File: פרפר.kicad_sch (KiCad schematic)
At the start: 41 parts, among them J1 JST_SH_BM03B-SRSS-TB, J2 Hirose_FH12-22S-0.5SH, J5 JST_SH_SM04B-SRSS-TB, J6 JST_SUR_SM02B-SURS-TF, J7 JST_SH_BM03B-SRSS-TB

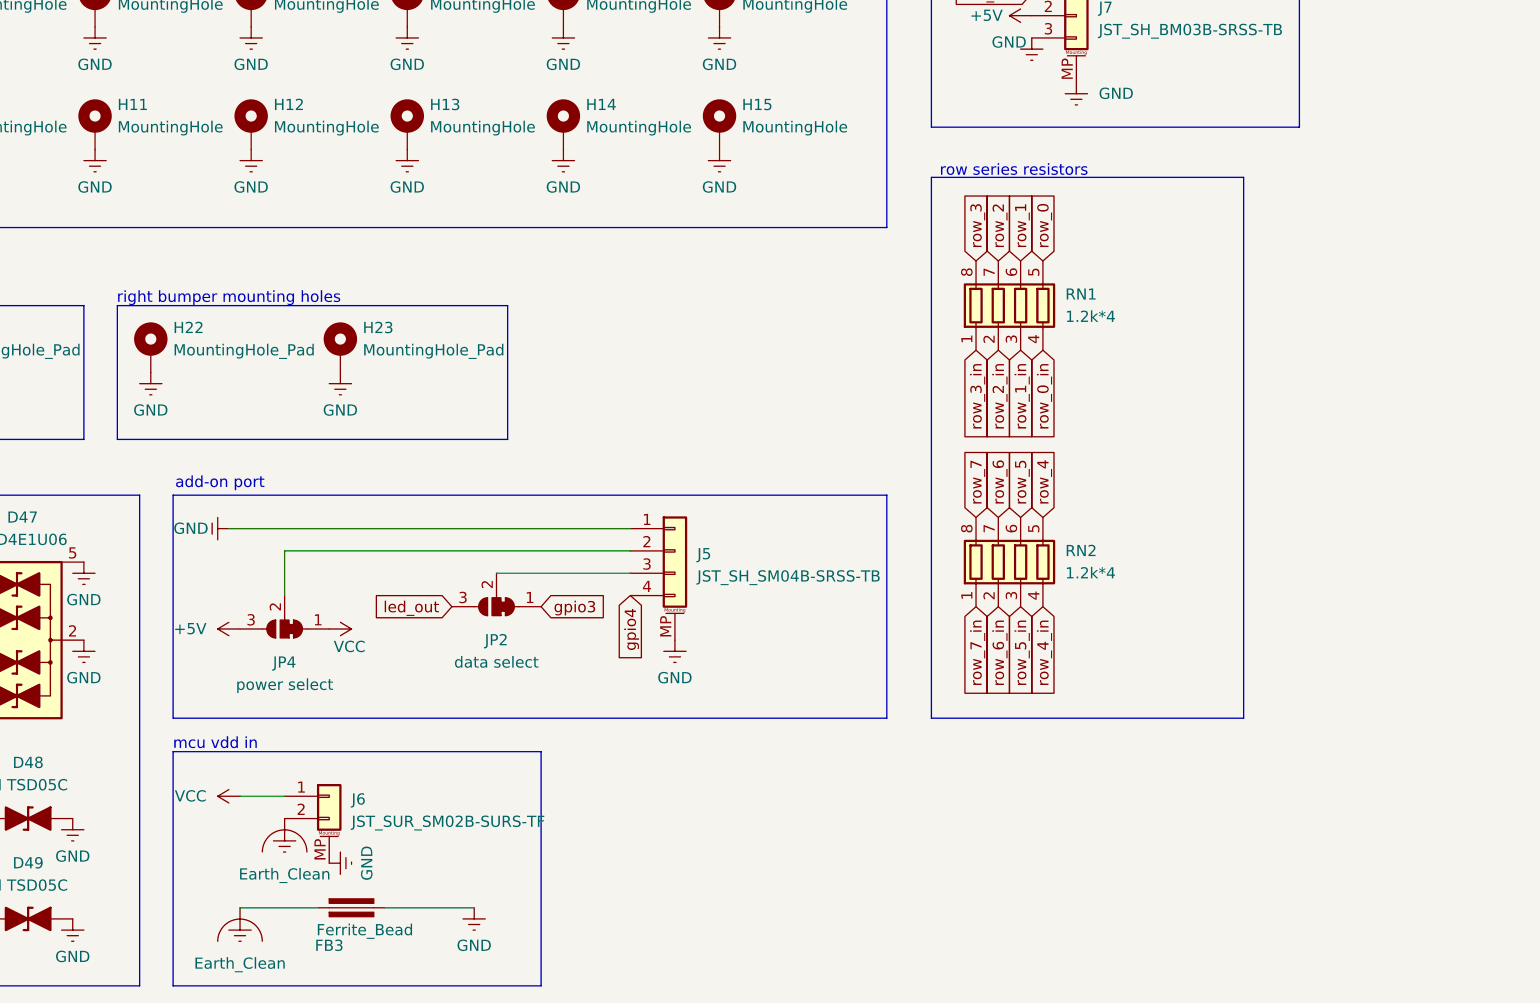
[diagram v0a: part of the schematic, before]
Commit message: column resistors to further bolster protection against esd events and shorts
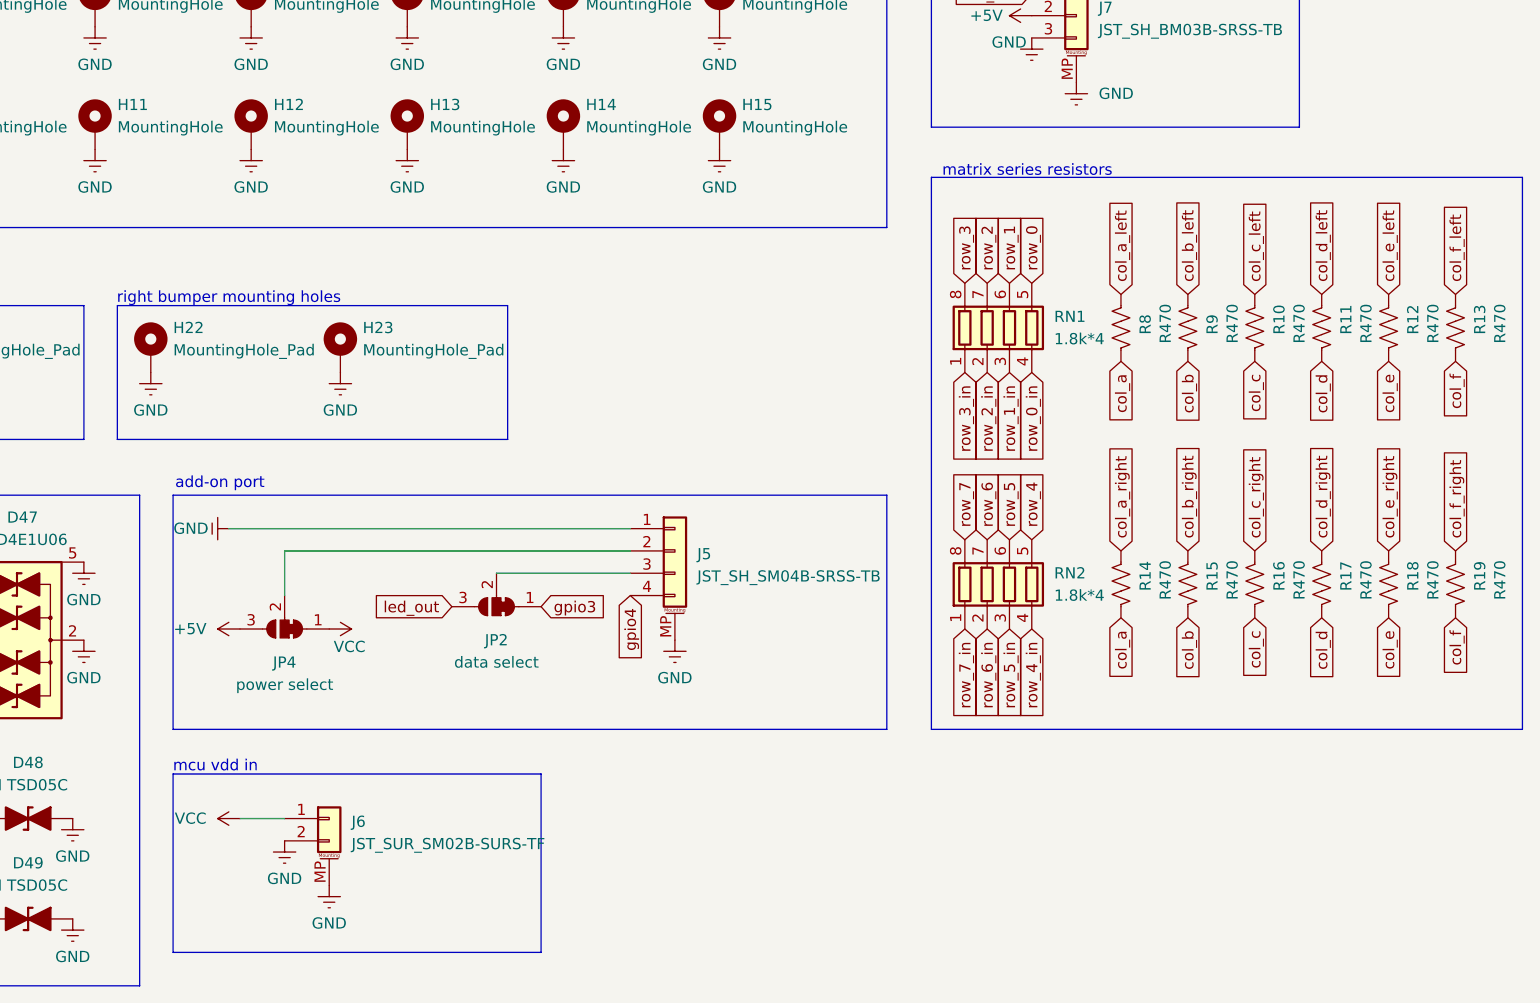
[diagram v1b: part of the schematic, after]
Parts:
- removed FB3: Ferrite_Bead, PCM_Ferrite_SMD_AKL:Ferrite_0805_2012Metric, symbol PCM_Device_AKL:Ferrite_Bead
- added R10, R11, R12, R13, R14, R15, R16, R17, R18, R19, R8, R9: R470, Resistor_SMD:R_0805_2012Metric, symbol Device:R_US
- RN1, RN2: value 1.2k*4 -> 1.8k*4
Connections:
- net Earth_Clean is gone; now on net GND: J6.2 (Pin_2)
- net col_a: now also R14.1, R8.1
- net col_b: now also R15.1, R9.1
- net col_c: now also R10.1, R16.1
- net col_d: now also R11.1, R17.1
- net col_e: now also R12.1, R18.1
- net col_f: now also R13.1, R19.1
- new net col_a_left: R8.2
- new net col_a_right: R14.2
- new net col_b_left: R9.2
- new net col_b_right: R15.2
- new net col_c_left: R10.2
- new net col_c_right: R16.2
- new net col_d_left: R11.2
- new net col_d_right: R17.2
- new net col_e_left: R12.2
- new net col_e_right: R18.2
- new net col_f_left: R13.2
- new net col_f_right: R19.2
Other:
- note added: "matrix series resistors"
- note removed: "row series resistors"
- moved on the sheet: J6, RN1, RN2

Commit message: actually production version, for real?
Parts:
- R10, R11, R12, R13, R14, R15, R16, R17, R18, R19, R8, R9: value R470 -> R220
- RN1, RN2: value 1.8k*4 -> R390*4
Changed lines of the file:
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@@
 	(title_block
 		(title "coquette switch matrix (parpar)")
-		(date "2025-01-20")
+		(date "2025-01-21")
 		(rev "2.0")
 	)
@@
 			)
 		)
-		(property "Value" "R470"
+		(property "Value" "R220"
 			(at 280.67 117.348 90)
 			(effects
@@
 			)
 		)
-		(property "Value" "R470"
+		(property "Value" "R220"
 			(at 280.67 146.558 90)
 			(effects
@@
 			)
 		)
-		(property "Value" "R470"
+		(property "Value" "R220"
 			(at 250.19 146.558 90)
 			(effects
@@
 			)
 		)
-		(property "Value" "1.8k*4"
+		(property "Value" "R390*4"
 			(at 229.87 116.8399 0)
 			(effects
@@
 			)
 		)
-		(property "Value" "R470"
+		(property "Value" "R220"
 			(at 250.19 117.348 90)
 			(effects
@@
 			)
 		)
-		(property "Value" "R470"
+		(property "Value" "R220"
 			(at 257.81 117.348 90)
 			(effects
@@
 			)
 		)
-		(property "Value" "R470"
+		(property "Value" "R220"
 			(at 242.57 117.348 90)
 			(effects
@@
 			)
 		)
-		(property "Value" "R470"
+		(property "Value" "R220"
 			(at 273.05 117.348 90)
 			(effects
@@
 			)
 		)
-		(property "Value" "R470"
+		(property "Value" "R220"
 			(at 242.57 146.558 90)
 			(effects
@@
 			)
 		)
-		(property "Value" "R470"
+		(property "Value" "R220"
 			(at 257.81 146.558 90)
 			(effects
@@
 			)
 		)
-		(property "Value" "R470"
+		(property "Value" "R220"
 			(at 273.05 146.558 90)
 			(effects
@@
 			)
 		)
-		(property "Value" "1.8k*4"
+		(property "Value" "R390*4"
 			(at 229.87 146.0499 0)
 			(effects
@@
 			)
 		)
-		(property "Value" "R470"
+		(property "Value" "R220"
 			(at 265.43 146.558 90)
 			(effects
@@
 			)
 		)
-		(property "Value" "R470"
+		(property "Value" "R220"
 			(at 265.43 117.348 90)
 			(effects

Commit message: v2 final ready to order
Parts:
- removed D1, D2, D45, D46, D47: TPD4E1U06, PCM_Package_TO_SOT_SMD_AKL:SOT-363_SC-70-6, symbol coquette_symbols:TPD4E1U06
- removed D48, D49: TI TSD05C, PCM_Diode_SMD_AKL:D_SOD-323_TVS, symbol PCM_Diode_TVS_AKL:D_TVS_Bidirectional_Generic
- removed FB1, FB2: Ferrite_Bead, PCM_Ferrite_SMD_AKL:Ferrite_0805_2012Metric, symbol PCM_Device_AKL:Ferrite_Bead
- removed H12, H13, H14, H15, H7, H8: MountingHole, MountingHole:MountingHole_3.2mm_M3_DIN965_Pad, symbol Mechanical:MountingHole_Pad
- removed H20, H21, H22, H23: MountingHole_Pad, MountingHole:MountingHole_2.2mm_M2_DIN965_Pad, symbol Mechanical:MountingHole_Pad
- removed J1, J7: JST_SH_BM03B-SRSS-TB, Connector_JST:JST_SH_BM03B-SRSS-TB_1x03-1MP_P1.00mm_Vertical, symbol Connector_Generic_MountingPin:Conn_01x03_MountingPin
- removed J6: JST_SUR_SM02B-SURS-TF, Connector_JST:JST_SUR_SM02B-SURS-TF_1x02-1MP_P0.80mm_Horizontal, symbol Connector_Generic_MountingPin:Conn_01x02_MountingPin
- removed JP2: data select, Jumper:SolderJumper-3_P1.3mm_Bridged12_RoundedPad1.0x1.5mm, symbol Jumper:SolderJumper_3_Bridged12
- removed JP4: power select, Jumper:SolderJumper-3_P1.3mm_Bridged12_RoundedPad1.0x1.5mm, symbol Jumper:SolderJumper_3_Bridged12
- removed R10, R11, R12, R13, R14, R15, R16, R17, R18, R19, R8, R9: R220, Resistor_SMD:R_0805_2012Metric, symbol Device:R_US
- added RN1: 2*4.7k, Resistor_SMD:R_Array_Convex_2x0402, symbol PCM_Resistor_US_AKL:R_2x0603_Concave
- added RN2, RN3, RN6: 1k*4, PCM_Resistor_SMD_AKL:R_Array_Concave_4x0603, symbol PCM_Resistor_AKL:R_4x0603_Concave
- added RN7: 2*R33, PCM_Resistor_SMD_AKL:R_Array_Concave_2x0603, symbol PCM_Resistor_US_AKL:R_2x0603_Concave
- H1: renamed from H2; footprint MountingHole:MountingHole_3.2mm_M3_DIN965_Pad -> MountingHole:MountingHole_2.2mm_M2_DIN965_Pad
- H2: renamed from H16; footprint MountingHole:MountingHole_3.2mm_M3_DIN965_Pad -> MountingHole:MountingHole_2.2mm_M2_DIN965_Pad
- H3: renamed from H18; footprint MountingHole:MountingHole_3.2mm_M3_DIN965_Pad -> MountingHole:MountingHole_2.2mm_M2_DIN965_Pad
- H4: renamed from H17; footprint MountingHole:MountingHole_3.2mm_M3_DIN965_Pad -> MountingHole:MountingHole_2.2mm_M2_DIN965_Pad
- H5: renamed from H19; footprint MountingHole:MountingHole_3.2mm_M3_DIN965_Pad -> MountingHole:MountingHole_2.2mm_M2_DIN965_Pad
- H6: renamed from H9; footprint MountingHole:MountingHole_3.2mm_M3_DIN965_Pad -> MountingHole:MountingHole_2.2mm_M2_DIN965_Pad
- H7: renamed from H10; footprint MountingHole:MountingHole_3.2mm_M3_DIN965_Pad -> MountingHole:MountingHole_2.2mm_M2_DIN965_Pad
- H8: renamed from H11; footprint MountingHole:MountingHole_3.2mm_M3_DIN965_Pad -> MountingHole:MountingHole_2.2mm_M2_DIN965_Pad
- J2: value Hirose_FH12-22S-0.5SH -> Conn_01x28_MountingPin; footprint Connector_FFC-FPC:Hirose_FH12-22S-0.5SH_1x22-1MP_P0.50mm_Horizontal -> coquette_footprints:FFC-28; symbol Connector_Generic_Shielded:Conn_01x22_Shielded -> Connector_Generic_MountingPin:Conn_01x28_MountingPin
- RN4: renamed from RN1; value R390*4 -> 1k*4
- RN5: renamed from RN2; value R390*4 -> 1k*4
- renumbered H3 to H13, H4 to H14, H5 to H15, H6 to H16, J5 to J1
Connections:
- net GND: now also J2.25 (Pin_25), J2.26 (Pin_26); no longer J2.1 (Pin_1), J2.22 (Pin_22)
- net VCC: now also J1.2 (Pin_2), J2.27 (Pin_27), J2.28 (Pin_28), RN1.3 (R2.2), RN1.4 (R1.2)
- net col_a: now also RN2.1 (R1.1); no longer J2.9 (Pin_9)
- net col_b: now also RN2.2 (R2.1); no longer J2.10 (Pin_10)
- net col_c: now also RN2.3 (R3.1); no longer J2.11 (Pin_11)
- net col_d: now also RN2.4 (R4.1); no longer J2.12 (Pin_12)
- net col_e: now also RN3.2 (R2.1); no longer J2.13 (Pin_13)
- net col_f: now also RN3.1 (R1.1); no longer J2.14 (Pin_14)
- net row_0: now also RN5.8 (R1.2); no longer RN4.5 (R4.2)
- net row_1: now also RN5.7 (R2.2); no longer RN4.6 (R3.2)
- net row_2: now also RN5.6 (R3.2); no longer RN4.7 (R2.2)
- net row_3: now also RN5.5 (R4.2); no longer RN4.8 (R1.2)
- net row_4: now also RN4.5 (R4.2); no longer RN5.5 (R4.2)
- net row_5: now also RN4.6 (R3.2); no longer RN5.6 (R3.2)
- net row_6: now also RN4.7 (R2.2); no longer RN5.7 (R2.2)
- net row_7: now also RN4.8 (R1.2); no longer RN5.8 (R1.2)
- net sda: now reaches J1.3 (Pin_3)
- net sda: now also RN7.1 (R1.1)
- net ec1a renamed ch7
- net ch7: now also RN4.3 (R3.1)
- net ec1b renamed ch8
- net ch8: now also RN4.4 (R4.1)
- net ec2a renamed ch15
- net ch15: now also RN1.1 (R1.1), RN7.4 (R1.2)
- net ec2b renamed ch16
- net ch16: now also RN2.5 (R4.2)
- net gpio3 renamed ch6
- net ch6: now also RN4.2 (R2.1)
- net gpio4 renamed ch17
- net ch17: now also RN2.6 (R3.2); no longer J1.4 (Pin_4)
- net row_0_in renamed ch2
- net ch2: now also RN6.2 (R2.1); no longer RN4.4 (R4.1)
- net row_1_in renamed ch3
- net ch3: now also RN6.3 (R3.1); no longer RN4.3 (R3.1)
- net row_2_in renamed ch4
- net ch4: now also RN6.4 (R4.1); no longer RN4.2 (R2.1)
- net row_3_in renamed ch5
- net row_4_in renamed ch18
- net ch18: now also RN2.7 (R2.2); no longer RN5.4 (R4.1)
- net row_5_in renamed ch19
- net ch19: now also RN2.8 (R1.2); no longer RN5.3 (R3.1)
- net row_6_in renamed ch20
- net ch20: now also RN5.1 (R1.1); no longer RN5.2 (R2.1)
- net row_7_in renamed ch21
- net ch21: now also RN5.2 (R2.1); no longer RN5.1 (R1.1)
- new net ch1: J2.1 (Pin_1), RN6.1 (R1.1)
- new net ch10: J2.10 (Pin_10)
- new net ch11: J2.11 (Pin_11)
- new net ch12: J2.12 (Pin_12), RN3.7 (R2.2)
- new net ch13: J2.13 (Pin_13), RN3.8 (R1.2)
- new net ch14: J2.14 (Pin_14), RN1.2 (R2.1), RN7.3 (R2.2)
- new net ch22: J2.22 (Pin_22), RN5.3 (R3.1)
- new net ch23: J2.23 (Pin_23), RN5.4 (R4.1)
- new net ch24: J2.24 (Pin_24)
- new net ch9: J2.9 (Pin_9), RN3.6 (R3.2)
- new net enc_1a: RN6.8 (R1.2)
- new net enc_1b: RN6.7 (R2.2)
- new net enc_2a: RN6.5 (R4.2)
- new net enc_2b: RN6.6 (R3.2)
- new net row_8: RN3.3 (R3.1)
- new net scl: J1.4 (Pin_4), RN7.2 (R2.1)
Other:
- note removed: "esd protection"
- note removed: "left bumper mounting holes"
- note removed: "mcu vdd in"
- note removed: "rgb out"
- note removed: "right bumper mounting holes"
- moved on the sheet: H1, H13, H14, H15, H16, H2, H3, H4, H5, H6, H7, H8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

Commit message: outline
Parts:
- removed H13, H14, H15, H16: MountingHole, MountingHole:MountingHole_3.2mm_M3_DIN965_Pad, symbol Mechanical:MountingHole_Pad
- removed J1: JST_SH_SM04B-SRSS-TB, Connector_JST:JST_SH_SM04B-SRSS-TB_1x04-1MP_P1.00mm_Horizontal, symbol Connector_Generic_MountingPin:Conn_01x04_MountingPin
- removed J2: Conn_01x28_MountingPin, coquette_footprints:FFC-28, symbol Connector_Generic_MountingPin:Conn_01x28_MountingPin
- removed RN1: 2*4.7k, Resistor_SMD:R_Array_Convex_2x0402, symbol PCM_Resistor_US_AKL:R_2x0603_Concave
- removed RN2, RN3, RN4, RN5, RN6: 1k*4, PCM_Resistor_SMD_AKL:R_Array_Concave_4x0603, symbol PCM_Resistor_AKL:R_4x0603_Concave
- removed RN7: 2*R33, PCM_Resistor_SMD_AKL:R_Array_Concave_2x0603, symbol PCM_Resistor_US_AKL:R_2x0603_Concave
- H1, H2, H3, H4, H5, H6, H7, H8: footprint MountingHole:MountingHole_2.2mm_M2_DIN965_Pad -> coquette_footprints:hex flange m2
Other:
- note removed: "add-on port"
- note removed: "input from mcu"
- note removed: "matrix series resistors"
- note removed: "mcu mounting holes"
